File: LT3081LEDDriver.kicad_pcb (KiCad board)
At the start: 2 copper layers, 50.8 x 82.6 mm, 75 parts, among them J1 V_{IN}, J10 +5V_{IN}, J11 LED, J2 PosIMon, J3 PosTempMon, J4 V_{LED}, J5 I2C, J6 Screw_Terminal_01x01, J7 Screw_Terminal_01x01, J8 Screw_Terminal_01x01, J9 Screw_Terminal_01x01, Q1 Q_NMOS_GSD, Q2 Q_NMOS_GSD, Q3 Q_NMOS_GDSD, U1 LT3081-DPAK-7, U2 INA219AxD, U3 DACx0501, U4 LTC4440ES6

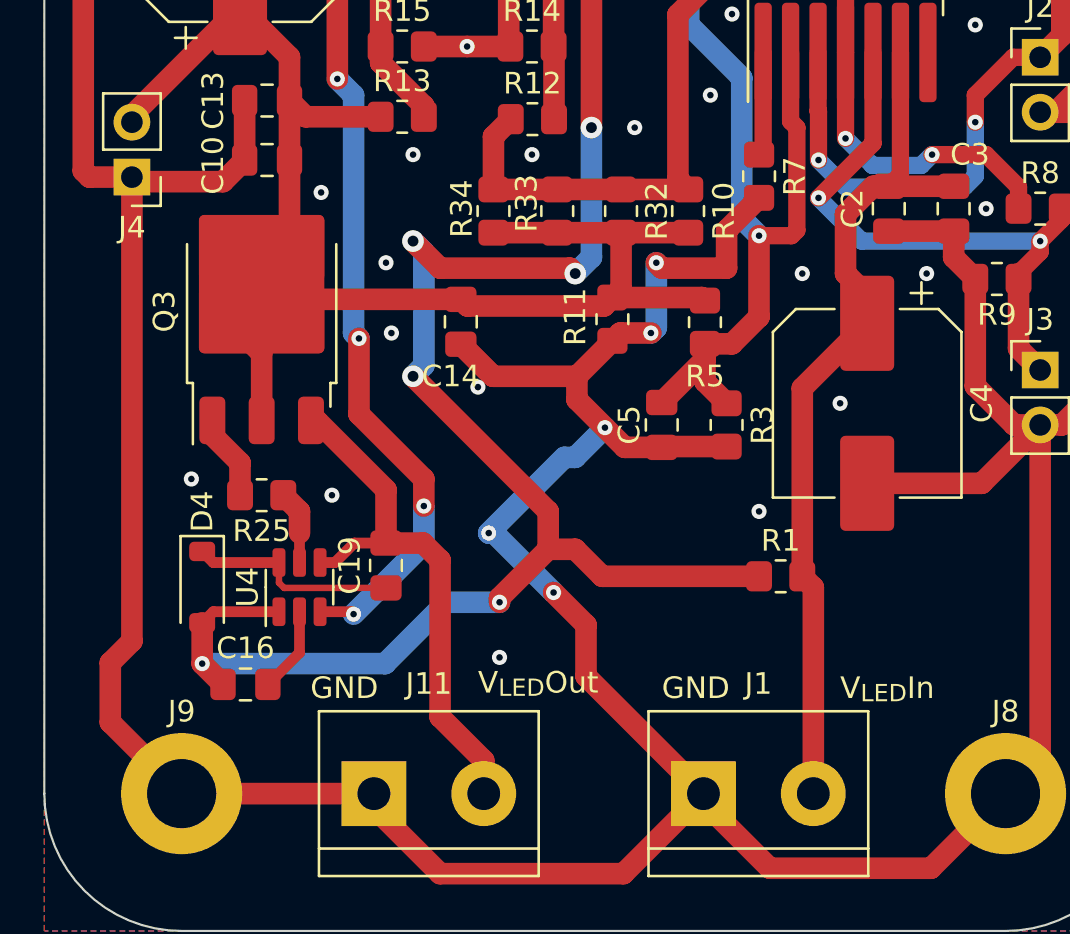
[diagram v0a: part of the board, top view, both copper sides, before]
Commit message: Added output capacitor to allow for smoothing of output voltage spike and an additional protection diode.
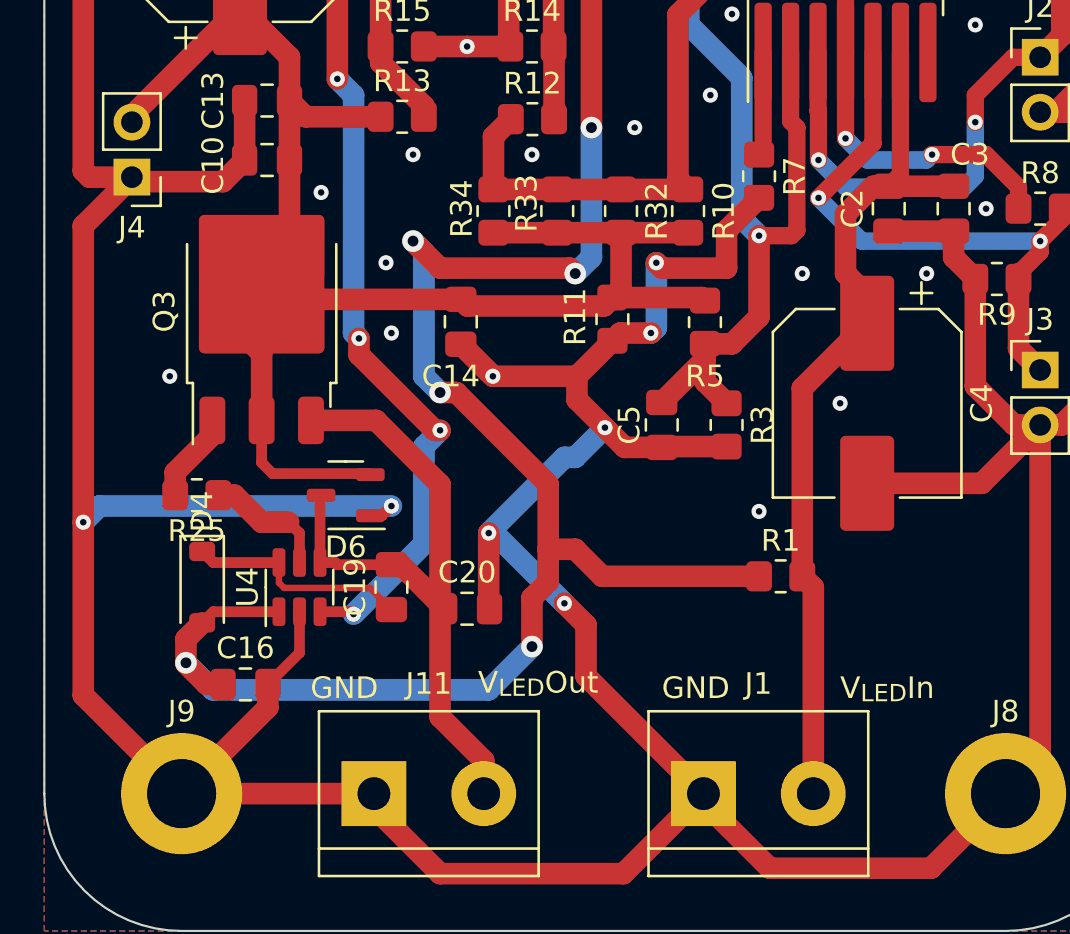
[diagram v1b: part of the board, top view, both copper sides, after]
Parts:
- added C20: 1nF, Capacitor_SMD:C_0805_2012Metric_Pad1.18x1.45mm_HandSolder, F.Cu at (127.5, 137.5)
- added D6: 100V, Package_TO_SOT_SMD:SOT-23-3, F.Cu at (121.9, 132.2)
- R11: value 1kΩ -> 10kΩ
- moved R25 3.00 mm to (115.0, 132.2)
- moved C19 1.03 mm to (124.0, 136.5)
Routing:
- net GND: track 510.0 -> 537.0 mm
- net /LT3081CurrentSupply/V_{LED}: track 61.2 -> 68.4 mm
- net Net-(D6-A): track 25.1 -> 32.1 mm
- net +5V: track 188.6 -> 193.5 mm
- net Net-(U4-TG): track 3.42 -> 5.84 mm
- net /HighSideGateDriver/TRIG: track 67.9 -> 68.7 mm
- net Net-(D4-K): track 9.75 -> 10.4 mm
